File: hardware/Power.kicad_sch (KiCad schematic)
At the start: 35 parts, among them IC1 TPS54202HDDCR, Q1 SI2347DS-T1-GE3, T10 TP_+5V, T11 TP_+5V, T3 TP_VCC, T8 TP_VCC, T9 TP_+3V3, U2 LM1117-3.3

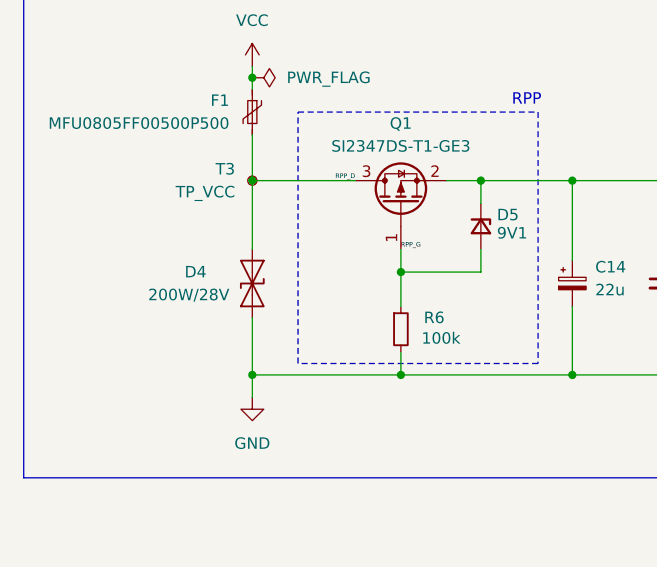
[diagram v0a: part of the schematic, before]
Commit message: changed out of stock parts
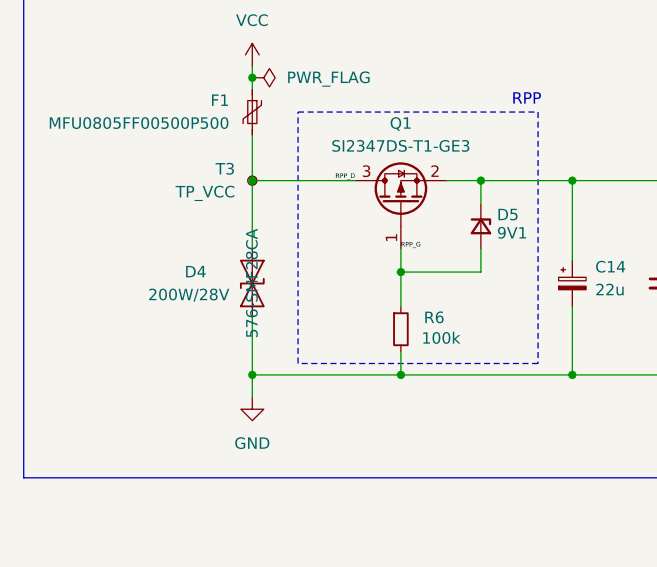
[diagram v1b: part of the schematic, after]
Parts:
- C14, C16: Mouser part number (none) -> 647-UCM1V220MCL1GS
- C15, C19: footprint Capacitor_SMD:C_0603_1608Metric_Pad1.08x0.95mm_HandSolder -> Capacitor_SMD:C_0805_2012Metric_Pad1.18x1.45mm_HandSolder; Mouser Price/Stock https://www.mouser.pl/ProductDetail/Murata-Electronics/GRM1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 -> https://www.mouser.pl/pl/ProductDetail/TDK/C2012X5R1V106M08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; Mouser part number (none) -> 810-C2012X5R1V106M0C
- C24, C29, C30, C31: Mouser Part Number 810-C2012X5R1V226MAC -> 81-ZRA21CR61E226ME1L; Mouser Price/Stock https://www.mouser.pl/ProductDetail/TDK/C2012X5R1V226M125AC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 -> https://www.mouser.pl/pl/ProductDetail/Murata-Electronics/Z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
- C25: Manufacturer_Part_Number C0603C104J3RACTU -> MAJCU168BB7104KTEA01; Mouser Part Number 80-C0603C104J3R -> 963-MAJCU168BB7104KT; Mouser Price/Stock https://www.mouser.pl/ProductDetail/Murata-Electronics/GRM0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 -> https://www.mouser.pl/pl/ProductDetail/TAIYO-YUDEN/MAJCU168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
- C26, C28: Mouser  part number (none) -> 963-MAJCU168BB7104KT; Mouser Price/Stock https://www.mouser.pl/ProductDetail/Murata-Electronics/GRM0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 -> https://www.mouser.pl/pl/ProductDetail/TAIYO-YUDEN/MAJCU168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
- C27: Manufacturer_Name (none) -> --; Manufacturer_Part_Number (none) -> MAJCU168BB7104KTEA01; Mouser Part Number (none) -> 963-MAJCU168BB7104KT; Mouser Price/Stock https://www.mouser.pl/ProductDetail/Murata-Electronics/GRM0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 -> https://www.mouser.pl/pl/ProductDetail/TAIYO-YUDEN/MAJCU168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
- C36: Mouser Price/Stock https://www.mouser.pl/ProductDetail/Murata-Electronics/GRM1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 -> https://www.mouser.pl/pl/ProductDetail/Samsung-Electro-Mech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; Mouser part number (none) -> 187-CL10A106MA8NRWC
- C37: Mouser Price/Stock https://www.mouser.pl/ProductDetail/TDK/C2012X5R1V226M125AC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 -> https://www.mouser.pl/pl/ProductDetail/Murata-Electronics/Z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; Mouser part number (none) -> 81-ZRA21CR61E226ME1L
- D4: Mouser part number (none) -> 576-SMF28CA
- D5: Mouser Price/Stock https://eu.mouser.com/ProductDetail/Micro-Commercial-Components-MCC/MMXZ5239B-TP?qs=ZNK0BnemlqF4shEFWztjGQ%3D%3D -> https://eu.mouser.com/ProductDetail/Micro-Commercial-Components-MCC/MMXhttps://www.mouser.pl/pl/ProductDetail/onsemi/SZMM3Z9V1T1G?qs=PJJcWtbOkNWOE7SiPfniZQ%3D%3DZ5239B-TP?qs=ZNK0BnemlqF4shEFWztjGQ%3D%3D; Mouser part number (none) -> 863-SZMM3Z9V1T1G
- F1: Mouser Price/Stock https://www.mouser.pl/ProductDetail/Vishay-Beyschlag/MFU080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 -> https://www.mouser.pl/pl/ProductDetail/Vishay-Beyschlag/MFU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; Mouser part number (none) -> 594-MFU0805FF00500P1
- Q1: Mouser part number (none) -> 78-SI2347DS-T1-GE3
- R6: Mouser part number (none) -> 660-RK73B1JTTD104J

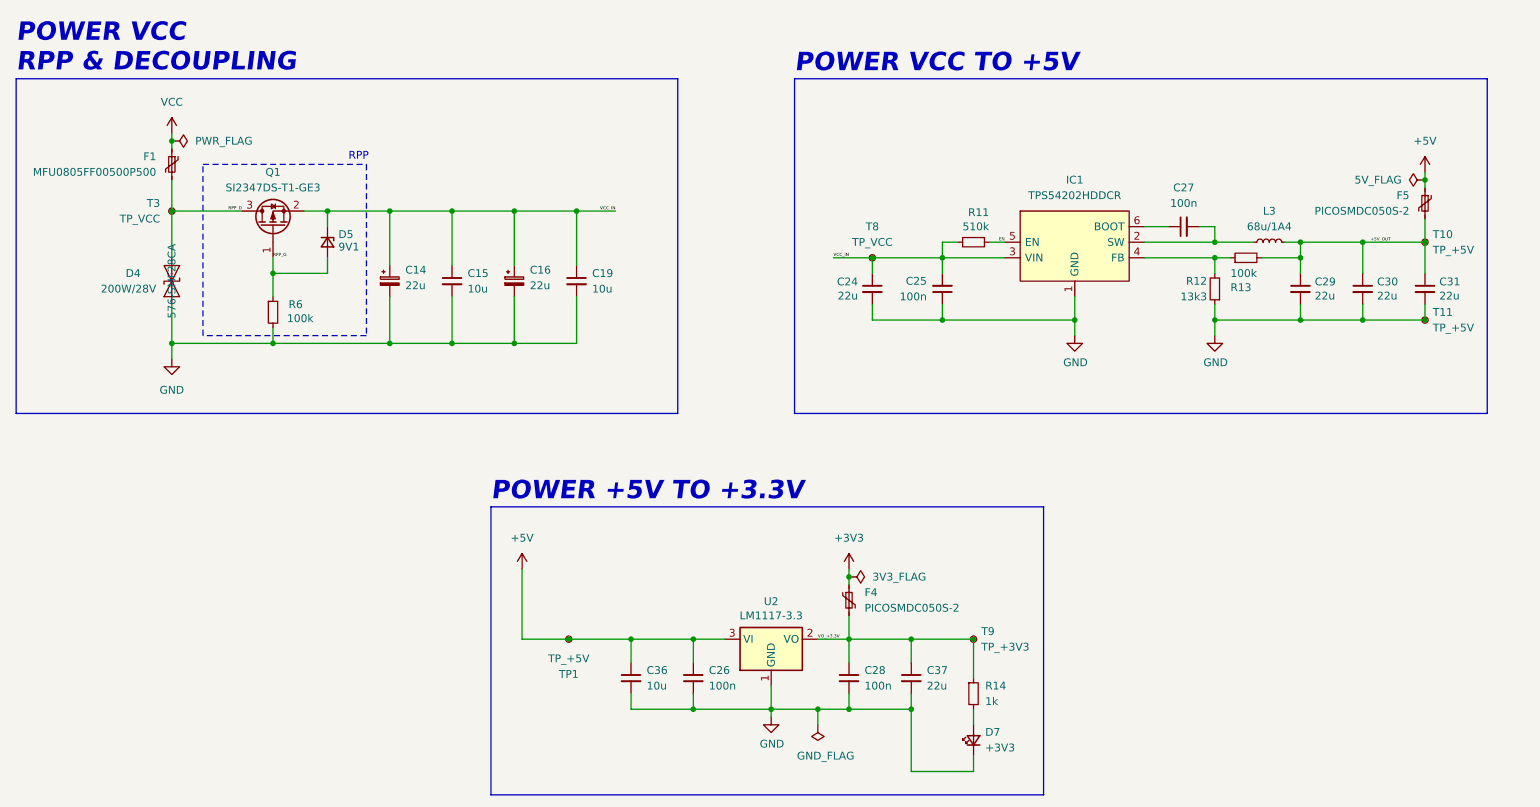
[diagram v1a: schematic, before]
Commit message: fixed mouser links
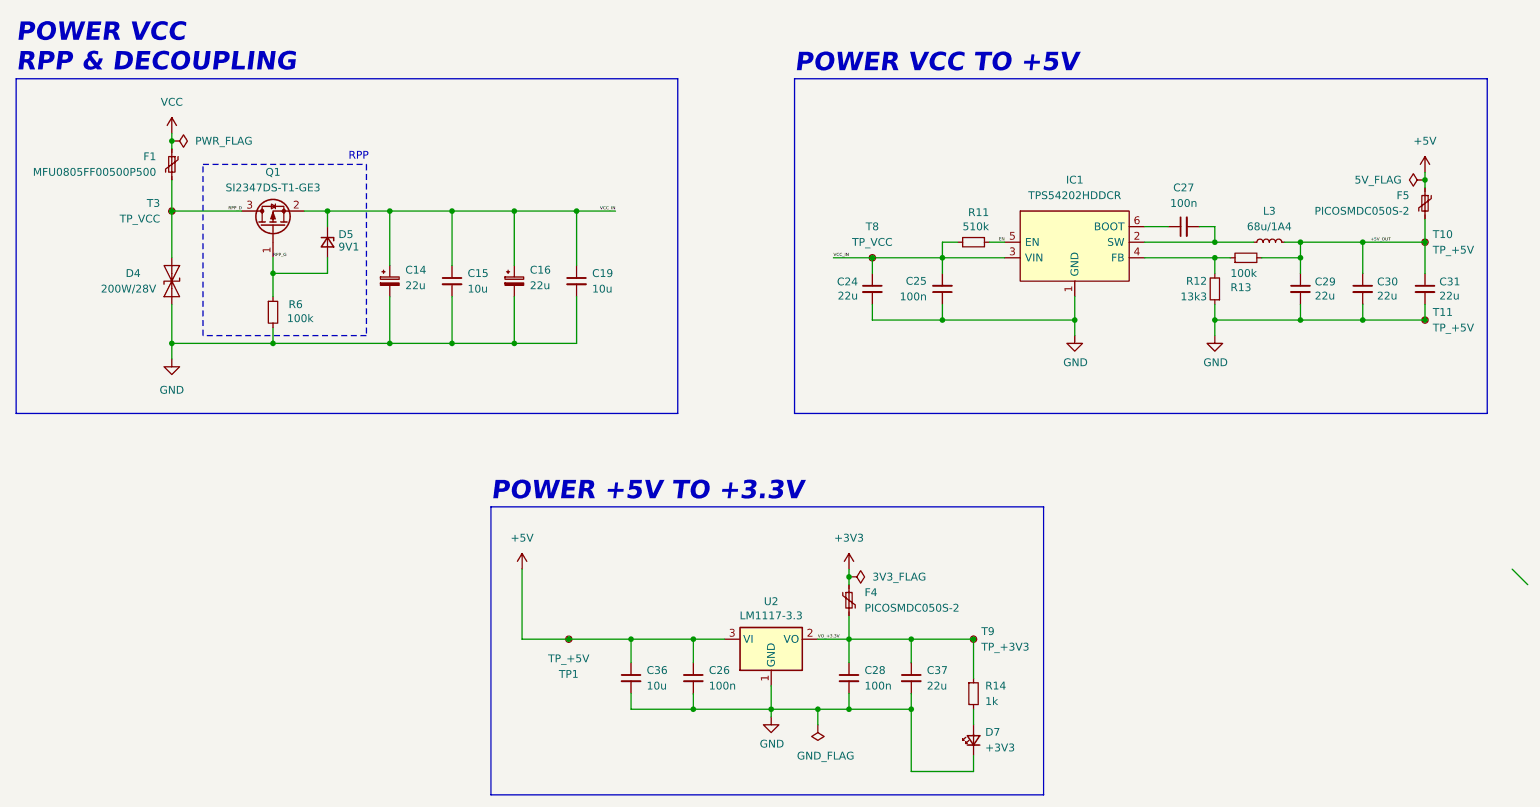
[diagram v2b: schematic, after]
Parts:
- R13: Mouser Part Number 603-RT0603DRE07100KL -> 660-RK73B1JTTD104J; Mouser Price/Stock https://www.mouser.pl/ProductDetail/KOA-Speer/RK73B1JTTD104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 -> https://www.mouser.pl/en/ProductDetail/KOA-Speer/RK73B1JTTD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
- R6: Mouser Price/Stock https://www.mouser.pl/ProductDetail/KOA-Speer/RK73B1JTTD104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 -> https://www.mouser.pl/en/ProductDetail/KOA-Speer/RK73B1JTTD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
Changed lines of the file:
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@@
 		(color 0 0 0 0)
 	)
+	(bus_entry
+		(at 268.224 114.3)
+		(size 2.54 2.54)
+		(stroke
+			(width 0)
+			(type default)
+		)
+	)
 	(wire
 		(pts
@@
 			)
 		)
-		(property "Mouser Price/Stock" "https://www.mouser.pl/ProductDetail/KOA-Speer/RK73B1JTTD104J?qs=sGAEpiMZZMvdGkrng054t2HaaJFon%252B0pQ1vDU7rpyKc%3D"
+		(property "Mouser Price/Stock" "https://www.mouser.pl/en/ProductDetail/KOA-Speer/RK73B1JTTD104J?qs=sGAEpiMZZMvdGkrng054t2HaaJFon%252B0pQ1vDU7rpyKc%3D"
 			(at 66.04 72.39 0)
 			(hide yes)
@@
 			)
 		)
-		(property "Mouser Part Number" "603-RT0603DRE07100KL"
+		(property "Mouser Part Number" "660-RK73B1JTTD104J"
 			(at 224.79 63.5 0)
 			(hide yes)
@@
 			)
 		)
-		(property "Mouser Price/Stock" "https://www.mouser.pl/ProductDetail/KOA-Speer/RK73B1JTTD104J?qs=sGAEpiMZZMvdGkrng054t2HaaJFon%252B0pQ1vDU7rpyKc%3D"
+		(property "Mouser Price/Stock" "https://www.mouser.pl/en/ProductDetail/KOA-Speer/RK73B1JTTD104J?qs=sGAEpiMZZMvdGkrng054t2HaaJFon%252B0pQ1vDU7rpyKc%3D"
 			(at 224.79 63.5 0)
 			(hide yes)
@@
 		(property "Mouser part number" "576-SMF28CA"
 			(at 49.53 67.31 0)
+			(hide yes)
 			(show_name no)
 			(do_not_autoplace no)
